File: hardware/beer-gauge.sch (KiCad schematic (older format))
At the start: 20 parts, among them J1 OLED_MODULE, P1 CONN_01X04, P2 CONN_01X04, P3 CONN_01X04, P4 CONN_01X04, U1 ADS1234IPW

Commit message: Working on footprints.  Exported netlist into layout.
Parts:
- W1, W2, W3, W4, W5, W6: footprint Measurement_Points:Measurement_Point_Round-TH_Small -> footprint:PadVia
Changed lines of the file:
@@
 $EndComp
 $Comp
-L +5V #PWR17
+L +5V #PWR01
 U 1 1 575B9063
 P 9600 2400
-F 0 "#PWR17" H 9600 2250 50  0001 C CNN
+F 0 "#PWR01" H 9600 2250 50  0001 C CNN
 F 1 "+5V" H 9600 2540 50  0000 C CNN
 F 2 "" H 9600 2400 50  0000 C CNN
@@
 $EndComp
 $Comp
-L +3.3V #PWR7
+L +3.3V #PWR02
 U 1 1 575B907B
 P 7800 2050
-F 0 "#PWR7" H 7800 1900 50  0001 C CNN
+F 0 "#PWR02" H 7800 1900 50  0001 C CNN
 F 1 "+3.3V" H 7800 2190 50  0000 C CNN
 F 2 "" H 7800 2050 50  0000 C CNN
@@
 $EndComp
 $Comp
-L GND #PWR8
+L GND #PWR03
 U 1 1 575B9093
 P 8000 4600
-F 0 "#PWR8" H 8000 4350 50  0001 C CNN
+F 0 "#PWR03" H 8000 4350 50  0001 C CNN
 F 1 "GND" H 8000 4450 50  0000 C CNN
 F 2 "" H 8000 4600 50  0000 C CNN
@@
 $EndComp
 $Comp
-L GND #PWR18
+L GND #PWR04
 U 1 1 575B9815
 P 9700 4400
-F 0 "#PWR18" H 9700 4150 50  0001 C CNN
+F 0 "#PWR04" H 9700 4150 50  0001 C CNN
 F 1 "GND" H 9700 4250 50  0000 C CNN
 F 2 "" H 9700 4400 50  0000 C CNN
@@
 $EndComp
 $Comp
-L GND #PWR11
+L GND #PWR05
 U 1 1 575B9A5F
 P 8850 4300
-F 0 "#PWR11" H 8850 4050 50  0001 C CNN
+F 0 "#PWR05" H 8850 4050 50  0001 C CNN
 F 1 "GND" H 8850 4150 50  0000 C CNN
 F 2 "" H 8850 4300 50  0000 C CNN
@@
 $EndComp
 $Comp
-L +5V #PWR10
+L +5V #PWR06
 U 1 1 575BA1FA
 P 8750 2300
-F 0 "#PWR10" H 8750 2150 50  0001 C CNN
+F 0 "#PWR06" H 8750 2150 50  0001 C CNN
 F 1 "+5V" H 8750 2440 50  0000 C CNN
 F 2 "" H 8750 2300 50  0000 C CNN
@@
 $EndComp
 $Comp
-L +5V #PWR9
+L +5V #PWR07
 U 1 1 575BA2EA
 P 8200 2050
-F 0 "#PWR9" H 8200 1900 50  0001 C CNN
+F 0 "#PWR07" H 8200 1900 50  0001 C CNN
 F 1 "+5V" H 8200 2190 50  0000 C CNN
 F 2 "" H 8200 2050 50  0000 C CNN
@@
 $EndComp
 $Comp
-L +5V #PWR15
+L +5V #PWR08
 U 1 1 575BA474
 P 9200 1500
-F 0 "#PWR15" H 9200 1350 50  0001 C CNN
+F 0 "#PWR08" H 9200 1350 50  0001 C CNN
 F 1 "+5V" H 9200 1640 50  0000 C CNN
 F 2 "" H 9200 1500 50  0000 C CNN
@@
 $EndComp
 $Comp
-L GND #PWR16
+L GND #PWR09
 U 1 1 575BA4B7
 P 9200 1900
-F 0 "#PWR16" H 9200 1650 50  0001 C CNN
+F 0 "#PWR09" H 9200 1650 50  0001 C CNN
 F 1 "GND" H 9200 1750 50  0000 C CNN
 F 2 "" H 9200 1900 50  0000 C CNN
@@
 $EndComp
 $Comp
-L GND #PWR6
+L GND #PWR010
 U 1 1 575BA95F
 P 7250 4300
-F 0 "#PWR6" H 7250 4050 50  0001 C CNN
+F 0 "#PWR010" H 7250 4050 50  0001 C CNN
 F 1 "GND" H 7250 4150 50  0000 C CNN
 F 2 "" H 7250 4300 50  0000 C CNN
@@
 $EndComp
 $Comp
-L GND #PWR3
+L GND #PWR011
 U 1 1 575BBEBC
 P 4750 4300
-F 0 "#PWR3" H 4750 4050 50  0001 C CNN
+F 0 "#PWR011" H 4750 4050 50  0001 C CNN
 F 1 "GND" H 4750 4150 50  0000 C CNN
 F 2 "" H 4750 4300 50  0000 C CNN
@@
 NoConn ~ 4800 2500
 $Comp
-L +3.3V #PWR2
+L +3.3V #PWR012
 U 1 1 575BC1B4
 P 4700 2200
-F 0 "#PWR2" H 4700 2050 50  0001 C CNN
+F 0 "#PWR012" H 4700 2050 50  0001 C CNN
 F 1 "+3.3V" H 4700 2340 50  0000 C CNN
 F 2 "" H 4700 2200 50  0000 C CNN
@@
 DISP_RESET
 $Comp
-L +3.3V #PWR4
+L +3.3V #PWR013
 U 1 1 575BD30D
 P 5500 1050
-F 0 "#PWR4" H 5500 900 50  0001 C CNN
+F 0 "#PWR013" H 5500 900 50  0001 C CNN
 F 1 "+3.3V" H 5500 1190 50  0000 C CNN
 F 2 "" H 5500 1050 50  0000 C CNN
@@
 $EndComp
 $Comp
-L GND #PWR5
+L GND #PWR014
 U 1 1 575BD336
 P 5500 1450
-F 0 "#PWR5" H 5500 1200 50  0001 C CNN
+F 0 "#PWR014" H 5500 1200 50  0001 C CNN
 F 1 "GND" H 5500 1300 50  0000 C CNN
 F 2 "" H 5500 1450 50  0000 C CNN
@@
 	1600 5100 1600 5000
 $Comp
-L GND #PWR1
+L GND #PWR015
 U 1 1 5767AC62
 P 1600 5550
-F 0 "#PWR1" H 1600 5300 50  0001 C CNN
+F 0 "#PWR015" H 1600 5300 50  0001 C CNN
 F 1 "GND" H 1600 5400 50  0000 C CNN
 F 2 "" H 1600 5550 50  0000 C CNN
@@
 $EndComp
 $Comp
-L GND #PWR13
+L GND #PWR016
 U 1 1 5768007C
 P 8900 1900
-F 0 "#PWR13" H 8900 1650 50  0001 C CNN
+F 0 "#PWR016" H 8900 1650 50  0001 C CNN
 F 1 "GND" H 8900 1750 50  0000 C CNN
 F 2 "" H 8900 1900 50  0000 C CNN
@@
 	8900 1900 8900 1850
 $Comp
-L +3.3V #PWR12
+L +3.3V #PWR017
 U 1 1 57680447
 P 8900 1500
-F 0 "#PWR12" H 8900 1350 50  0001 C CNN
+F 0 "#PWR017" H 8900 1350 50  0001 C CNN
 F 1 "+3.3V" H 8900 1640 50  0000 C CNN
 F 2 "" H 8900 1500 50  0000 C CNN
@@
 $EndComp
 $Comp
-L GND #PWR14
+L GND #PWR018
 U 1 1 5766E726
 P 8950 6150
-F 0 "#PWR14" H 8950 5900 50  0001 C CNN
+F 0 "#PWR018" H 8950 5900 50  0001 C CNN
 F 1 "GND" H 8950 6000 50  0000 C CNN
 F 2 "" H 8950 6150 50  0000 C CNN
@@
 F 0 "W1" V 3650 6400 50  0000 C CNN
 F 1 "TEST_1P" H 3650 6350 50  0001 C CNN
-F 2 "Measurement_Points:Measurement_Point_Round-TH_Small" H 3850 6150 50  0001 C CNN
+F 2 "footprint:PadVia" H 3850 6150 50  0001 C CNN
 F 3 "" H 3850 6150 50  0000 C CNN
 	1    3650 6150
@@
 F 0 "W2" V 3650 6500 50  0000 C CNN
 F 1 "TEST_1P" H 3650 6450 50  0001 C CNN
-F 2 "Measurement_Points:Measurement_Point_Round-TH_Small" H 3850 6250 50  0001 C CNN
+F 2 "footprint:PadVia" H 3850 6250 50  0001 C CNN
 F 3 "" H 3850 6250 50  0000 C CNN
 	1    3650 6250
@@
 F 0 "W3" V 3650 6600 50  0000 C CNN
 F 1 "TEST_1P" H 3650 6550 50  0001 C CNN
-F 2 "Measurement_Points:Measurement_Point_Round-TH_Small" H 3850 6350 50  0001 C CNN
+F 2 "footprint:PadVia" H 3850 6350 50  0001 C CNN
 F 3 "" H 3850 6350 50  0000 C CNN
 	1    3650 6350
@@
 F 0 "W4" V 3650 6700 50  0000 C CNN
 F 1 "TEST_1P" H 3650 6650 50  0001 C CNN
-F 2 "Measurement_Points:Measurement_Point_Round-TH_Small" H 3850 6450 50  0001 C CNN
+F 2 "footprint:PadVia" H 3850 6450 50  0001 C CNN
 F 3 "" H 3850 6450 50  0000 C CNN
 	1    3650 6450
@@
 F 0 "W5" V 3650 6800 50  0000 C CNN
 F 1 "TEST_1P" H 3650 6750 50  0001 C CNN
-F 2 "Measurement_Points:Measurement_Point_Round-TH_Small" H 3850 6550 50  0001 C CNN
+F 2 "footprint:PadVia" H 3850 6550 50  0001 C CNN
 F 3 "" H 3850 6550 50  0000 C CNN
 	1    3650 6550
@@
 F 0 "W6" V 3650 6900 50  0000 C CNN
 F 1 "TEST_1P" H 3650 6850 50  0001 C CNN
-F 2 "Measurement_Points:Measurement_Point_Round-TH_Small" H 3850 6650 50  0001 C CNN
+F 2 "footprint:PadVia" H 3850 6650 50  0001 C CNN
 F 3 "" H 3850 6650 50  0000 C CNN
 	1    3650 6650

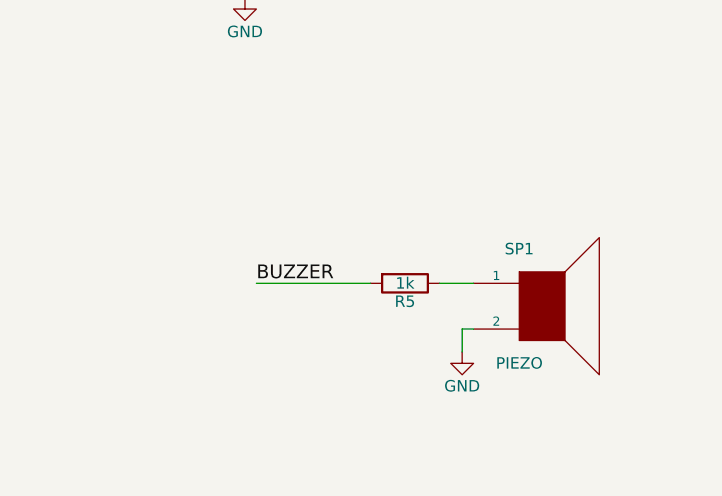
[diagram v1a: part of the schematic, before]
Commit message: Finished footprints.  Switched to a tantalum cap for the LCD.  Changed piezo resistor value to 470 to reduce part count.
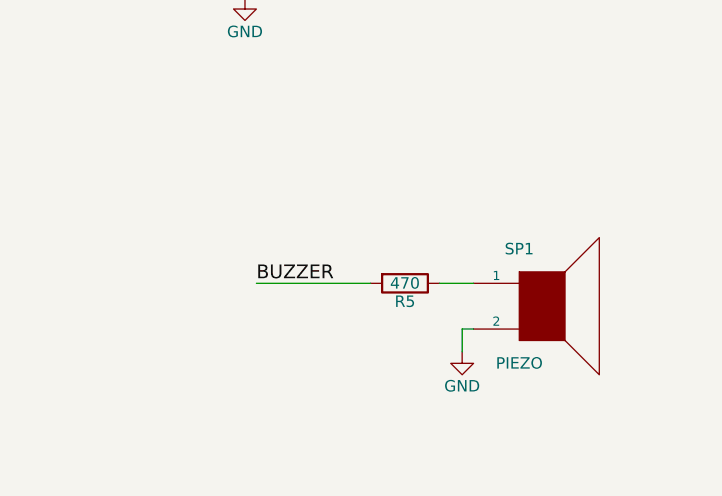
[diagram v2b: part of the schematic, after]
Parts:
- C1: footprint Capacitors_SMD:c_elec_6.3x5.8 -> Capacitors_Tantalum_SMD:TantalC_SizeD_EIA-7343_Reflow
- J1: footprint MODULE -> footprint:0522712069
- R5: value 1k -> 470
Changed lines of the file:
@@
 F 0 "J1" H 5150 4450 50  0000 C CNN
 F 1 "OLED_MODULE" H 5350 2050 50  0000 C CNN
-F 2 "MODULE" H 5550 3250 50  0001 C CNN
+F 2 "footprint:0522712069" H 5550 3250 50  0001 C CNN
 F 3 "DOCUMENTATION" H 5550 3250 50  0001 C CNN
 	1    5550 3250
@@
 F 0 "C1" H 5525 1350 50  0000 L CNN
 F 1 "220u" H 5525 1150 50  0000 L CNN
-F 2 "Capacitors_SMD:c_elec_6.3x5.8" H 5538 1100 50  0001 C CNN
+F 2 "Capacitors_Tantalum_SMD:TantalC_SizeD_EIA-7343_Reflow" H 5538 1100 50  0001 C CNN
 F 3 "" H 5500 1250 50  0000 C CNN
 	1    5500 1250
@@
 P 8700 5850
 F 0 "R5" V 8780 5850 50  0000 C CNN
-F 1 "1k" V 8700 5850 50  0000 C CNN
+F 1 "470" V 8700 5850 50  0000 C CNN
 F 2 "Resistors_SMD:R_0603" V 8630 5850 50  0001 C CNN
 F 3 "" H 8700 5850 50  0000 C CNN

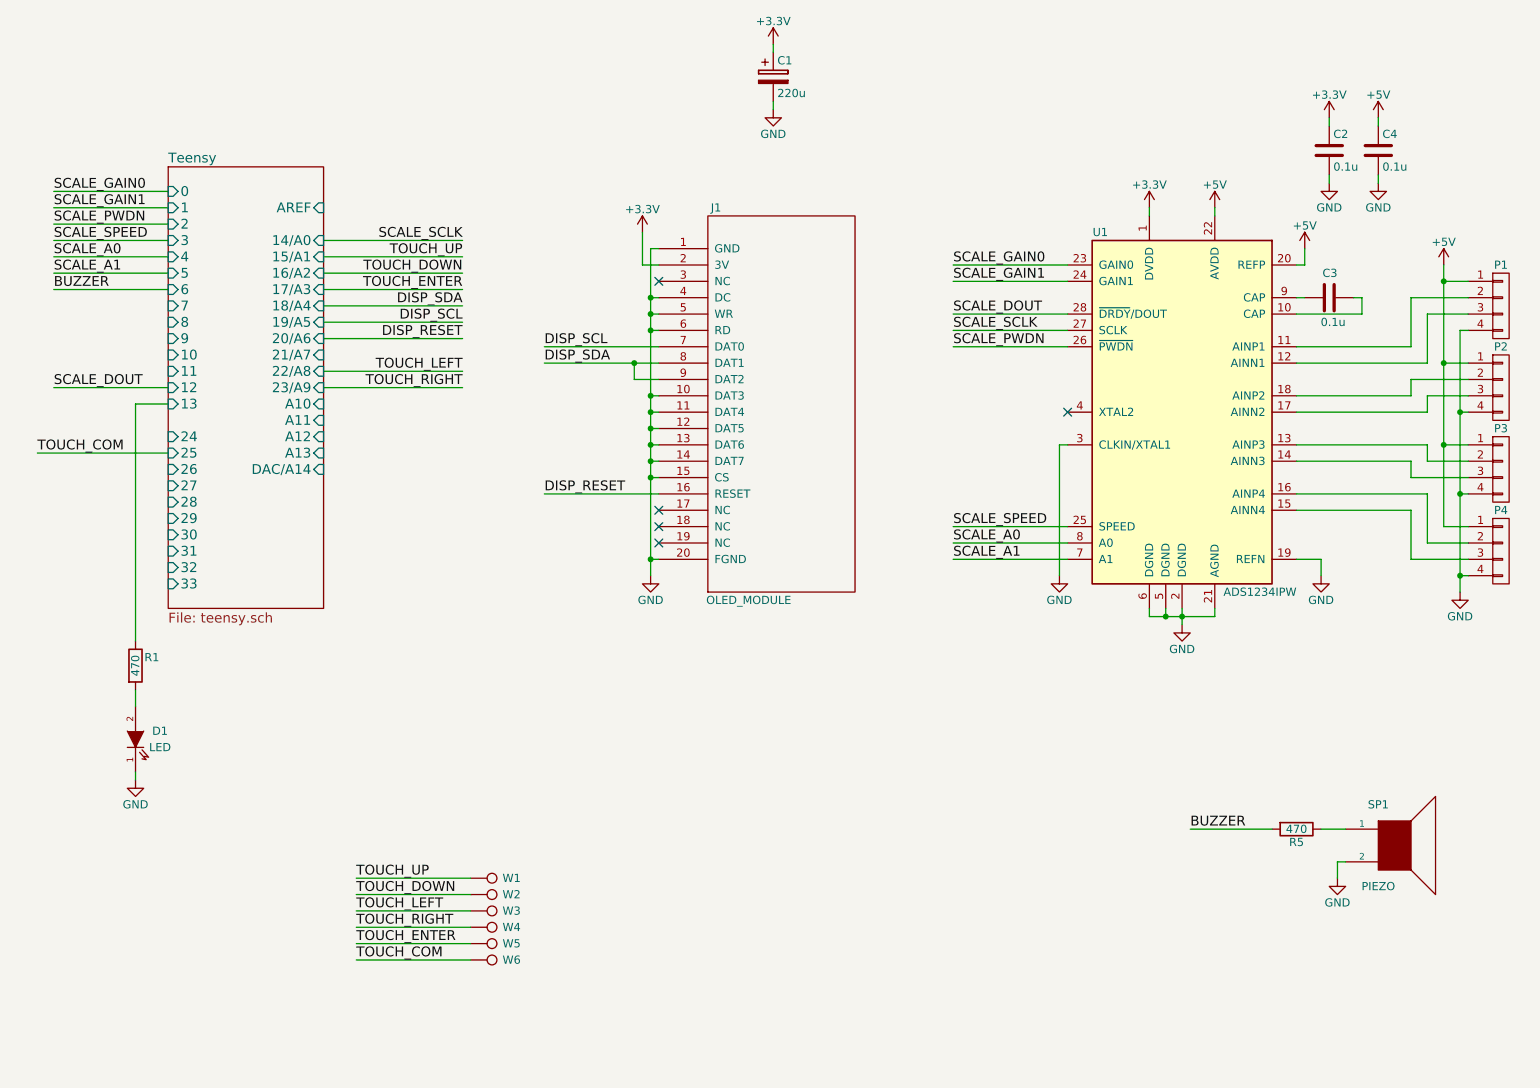
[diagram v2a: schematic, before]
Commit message: Changed OLED display to use SPI interface in schematic
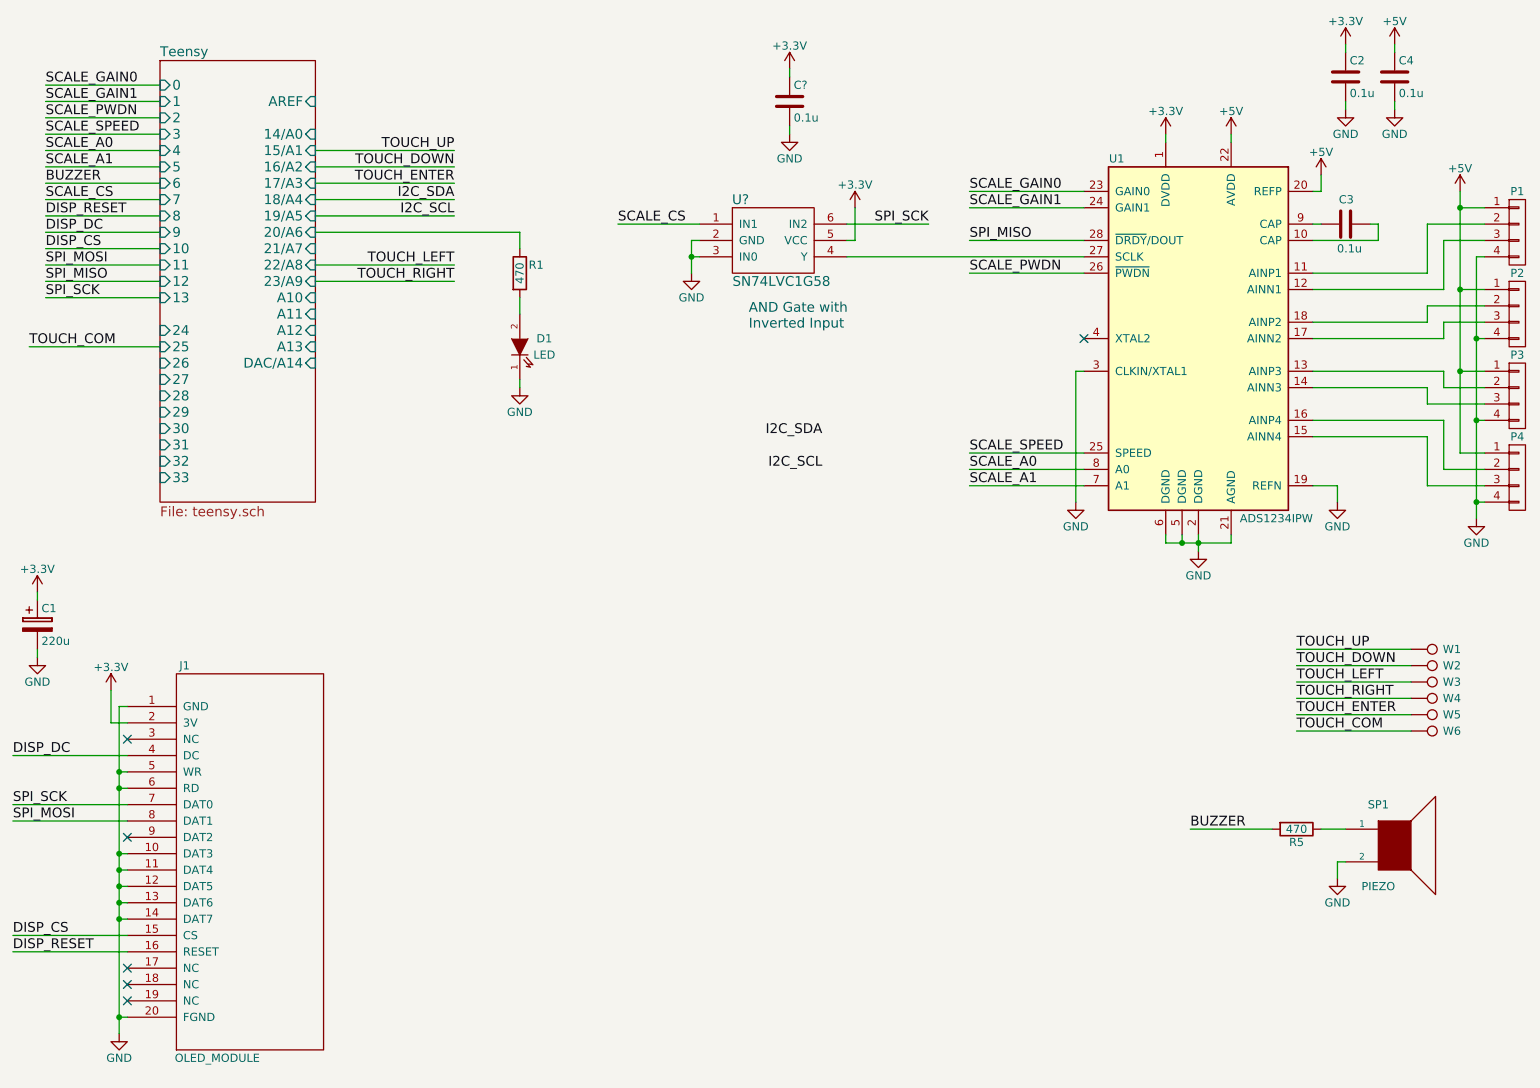
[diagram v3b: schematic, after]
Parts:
- added C?: 0.1u, Capacitors_SMD:C_0603, symbol C
- added U?: SN74LVC1G58, symbol SN74LVC1G58
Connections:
- net +3V3: now also C?.1, U?.5 (VCC)
- net GND: now also C?.2, U?.2 (GND), U?.3 (IN0); no longer J1.15 (CS), J1.4 (DC)
- net DISP_SCL renamed SPI_SCK
- net SPI_SCK: now also U?.6 (IN2)
- net DISP_SDA: no longer names the net of J1.9 (DAT2)
- net DISP_SDA: no longer J1.8 (DAT1)
- net SCALE_DOUT renamed SPI_MISO
- net SCALE_SCLK: no longer names the net of U1.27 (SCLK)
- net SCALE_SCLK: now also U?.4 (Y)
- net Teensy/13 renamed Teensy/20/A6
- new net DISP_CS: J1.15 (CS)
- new net DISP_DC: J1.4 (DC)
- new net SCALE_CS: U?.1 (IN1)
- new net SPI_MOSI: J1.8 (DAT1)
- no-connect marks 5 -> 6
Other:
- note added: "AND Gate with\nInverted Input"
- moved on the sheet: C1, C2, C3, C4, D1, J1, P1, P2, P3, P4, R1, U1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

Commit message: Updating schematic/BOM to use 2 channel ADC, added I2C switch
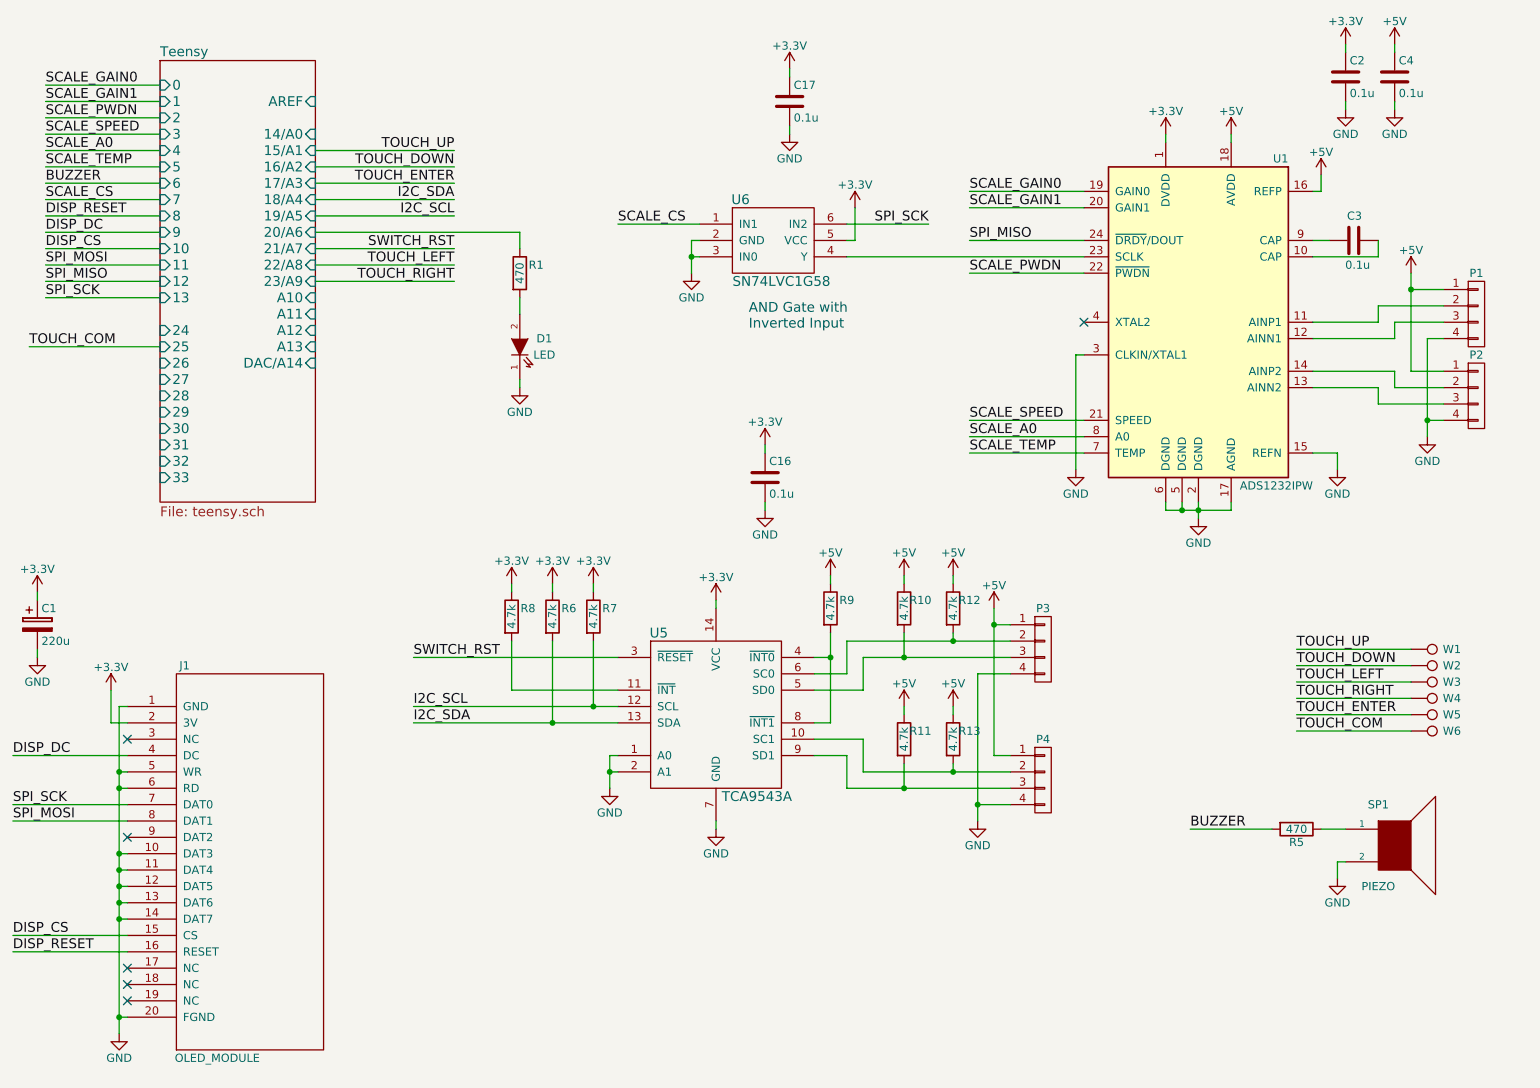
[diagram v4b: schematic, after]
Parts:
- removed U1: ADS1234IPW, Housings_SSOP:TSSOP-28_4.4x9.7mm_Pitch0.65mm, symbol ADS1234IPW
- added C16: 0.1u, Capacitors_SMD:C_0603, symbol C
- added R10, R11, R12, R13, R6, R7, R8, R9: 4.7k, Resistors_SMD:R_0603, symbol R
- added U1: ADS1232IPW, Housings_SSOP:TSSOP-24_4.4x7.8mm_Pitch0.65mm, symbol ADS1232IPW
- added U5: TCA9543A, Housings_SSOP:TSSOP-14_4.4x5mm_Pitch0.65mm, symbol TCA9543A
- U6: renamed from U?; footprint (none) -> TO_SOT_Packages_SMD:SC-70-6
- gave numbers to parts that had none: 1
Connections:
- net +3V3: now also C16.1, R6.1, R7.1, R8.1, U1.1 (DVDD), U5.14 (VCC)
- net +5V: now also R10.1, R11.1, R12.1, R13.1, R9.1, U1.16 (REFP), U1.18 (AVDD)
- net GND: now also C16.2, U1.15 (REFN), U1.17 (AGND), U1.2 (DGND), U1.3 (CLKIN/XTAL1), U1.5 (DGND), U1.6 (DGND), U5.1 (A0), U5.2 (A1), U5.7 (GND)
- net I2C_SCL: now also R7.2, U5.12 (SCL)
- net I2C_SDA: now also R6.2, U5.13 (SDA)
- net SCALE_A0: now also U1.8 (A0)
- net SCALE_GAIN0: now also U1.19 (GAIN0)
- net SCALE_GAIN1: now also U1.20 (GAIN1)
- net SCALE_PWDN: now also U1.22 (~PWDN~)
- net SCALE_SPEED: now also U1.21 (SPEED)
- net SPI_MISO: now also U1.24 (~DRDY~/DOUT)
- net at C3.2: now also U1.10 (CAP)
- net at P1.2 (P2): now also U1.11 (AINP1)
- net at P1.3 (P3): now also U1.12 (AINN1)
- net at P3.2 (P2): now also R12.2, U5.6 (SC0)
- net at P3.3 (P3): now also R10.2, U5.5 (SD0)
- net at P4.3 (P3): now also R11.2, U5.9 (SD1)
- net at P4.2 (P2): now also R13.2, U5.10 (SC1)
- net at P2.3 (P3): now also U1.13 (AINN2)
- net at P2.2 (P2): now also U1.14 (AINP2)
- net at U6.4 (Y): now also U1.23 (SCLK)
- net at C3.1: now also U1.9 (CAP)
- new net: R8.2, U5.11 (~INT)
- new net: R9.2, U5.4 (~INT0), U5.8 (~INT1)
- new net SCALE_TEMP: U1.7 (TEMP)
- new net SWITCH_RST: U5.3 (~RESET)
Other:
- moved on the sheet: C3, P1, P2, P3, P4
